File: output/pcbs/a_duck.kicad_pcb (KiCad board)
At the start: 2 copper layers, 135.1 x 107.9 mm, 38 parts

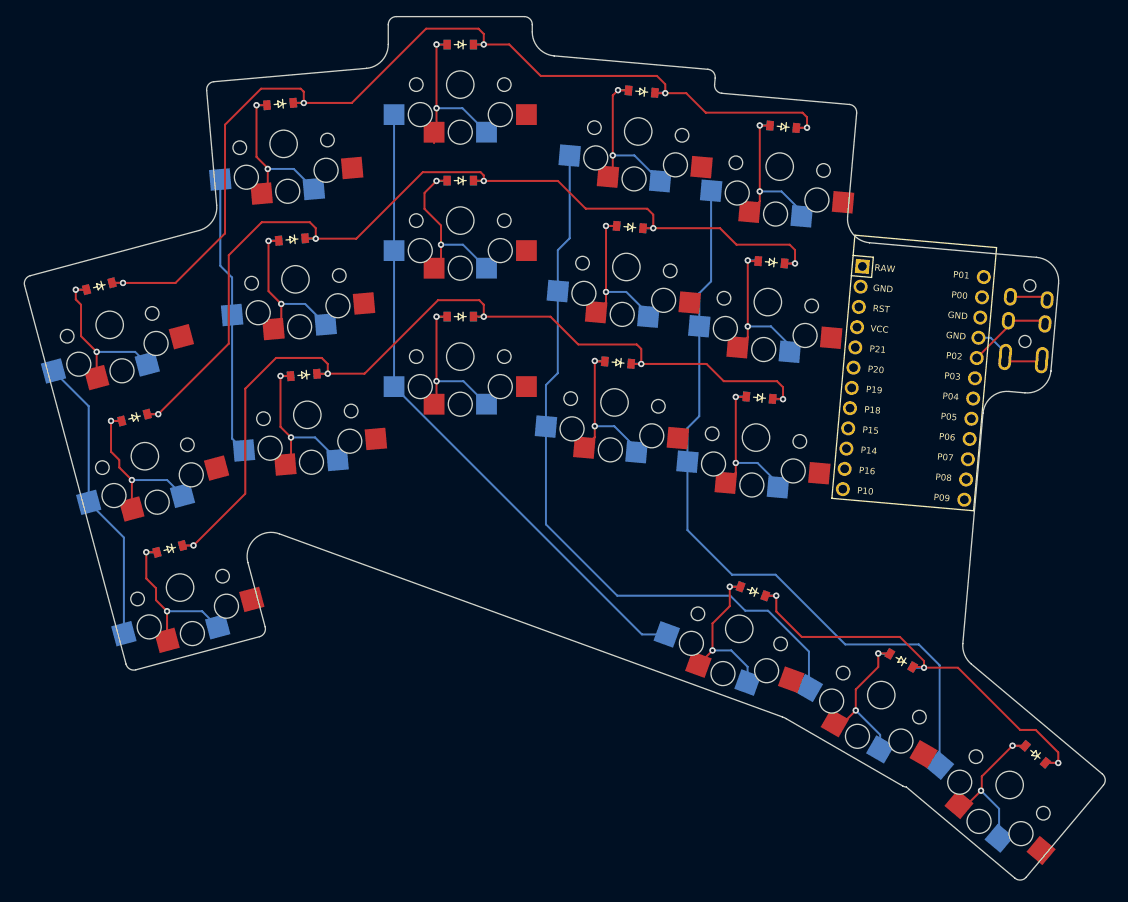
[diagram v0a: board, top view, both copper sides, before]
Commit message: Fix outlines / edge cuts of PCB
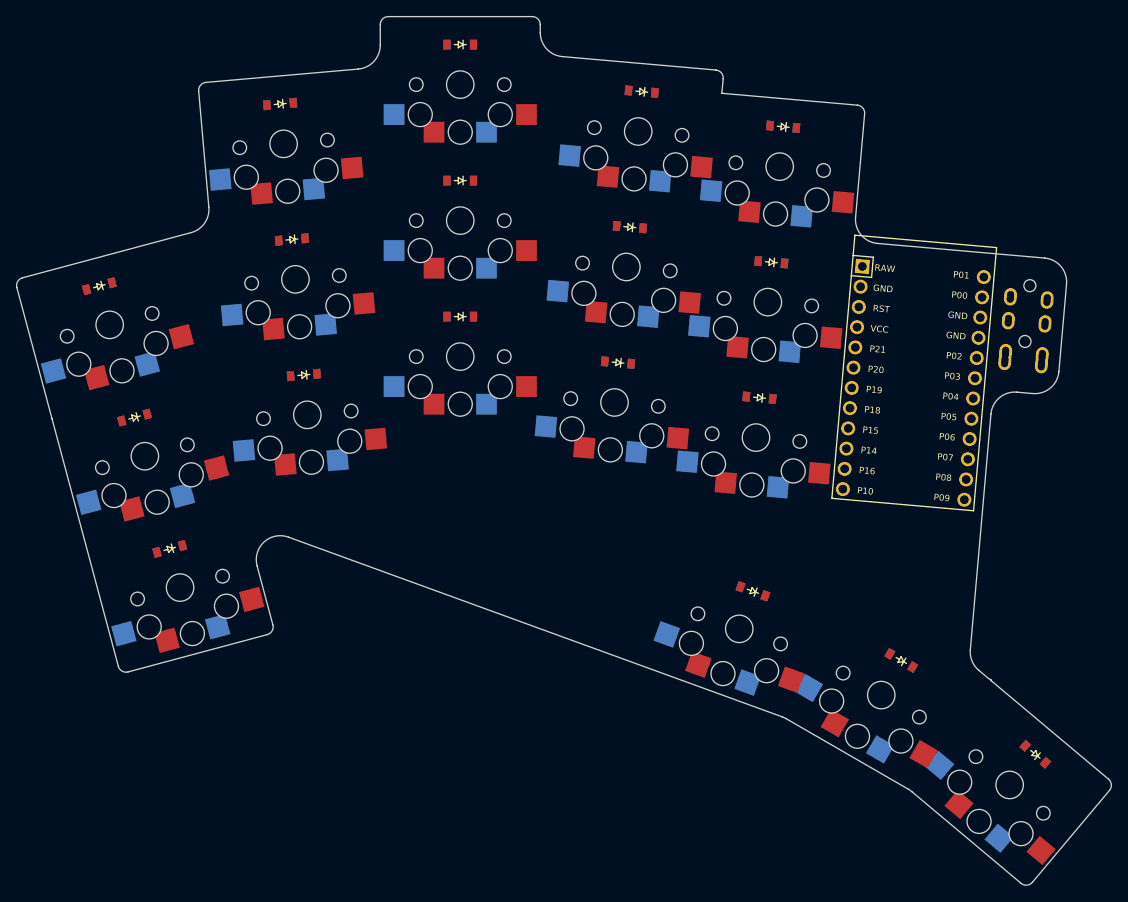
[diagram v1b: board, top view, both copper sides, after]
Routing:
- net P15: track 129.8 -> 0.00 mm, vias 5 -> 0
- net P14: track 121.9 -> 0.00 mm, vias 5 -> 0
- net P16: track 118.3 -> 0.00 mm, vias 5 -> 0
- net P5: track 94.7 -> 0.00 mm
- net P6: track 91.3 -> 0.00 mm
- net P7: track 81.3 -> 0.00 mm
- net P10: track 55.2 -> 0.00 mm, vias 3 -> 0
- net P9: track 38.2 -> 0.00 mm
- net P8: track 35.1 -> 0.00 mm
- net middle_top: track 24.3 -> 0.00 mm, vias 2 -> 0
- net middle_home: track 23.4 -> 0.00 mm, vias 2 -> 0
- net pinky_bottom: track 23.3 -> 0.00 mm, vias 2 -> 0
- net middle_bottom: track 22.9 -> 0.00 mm, vias 2 -> 0
- net pinky_home: track 21.9 -> 0.00 mm, vias 2 -> 0
- net pinky_top: track 21.7 -> 0.00 mm, vias 2 -> 0
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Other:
- board size 135.1 x 107.9 mm -> 136.8 x 108.6 mm

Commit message: Fix left side pins for easier routing
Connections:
- D1 pad 1: P16 -> P14
- D10 pad 1: P16 -> P14
- D11 pad 1: P14 -> P16
- D12 pad 1: P15 -> P10
- D13 pad 1: P16 -> P14
- D14 pad 1: P14 -> P16
- D15 pad 1: P15 -> P10
- D16 pad 1: P10 -> P15
- D17 pad 1: P10 -> P15
- D18 pad 1: P10 -> P15
- D2 pad 1: P14 -> P16
- D3 pad 1: P15 -> P10
- D4 pad 1: P16 -> P14
- D5 pad 1: P14 -> P16
- D6 pad 1: P15 -> P10
- D7 pad 1: P16 -> P14
- D8 pad 1: P14 -> P16
- D9 pad 1: P15 -> P10

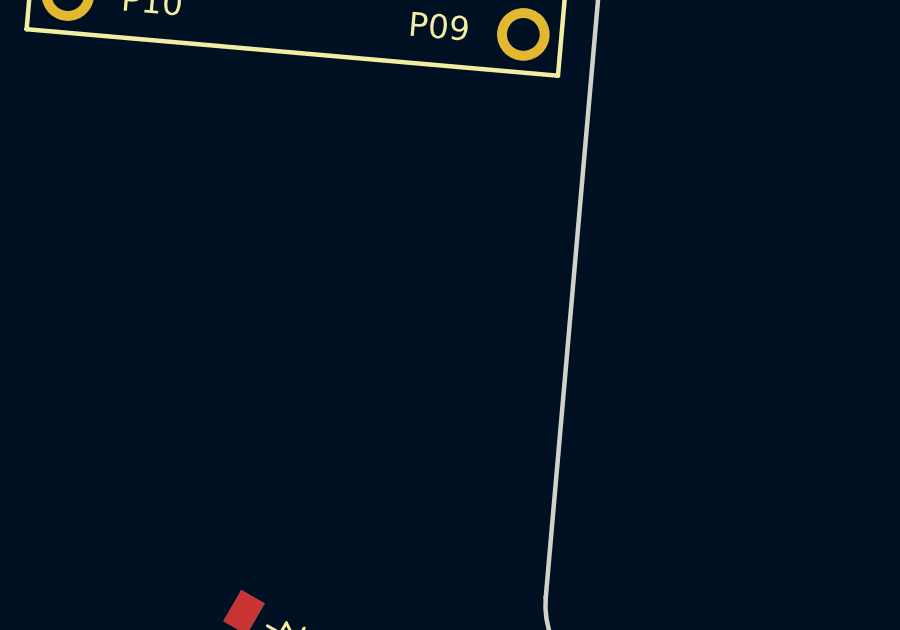
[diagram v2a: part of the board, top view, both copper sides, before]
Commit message: Added SMD reset button
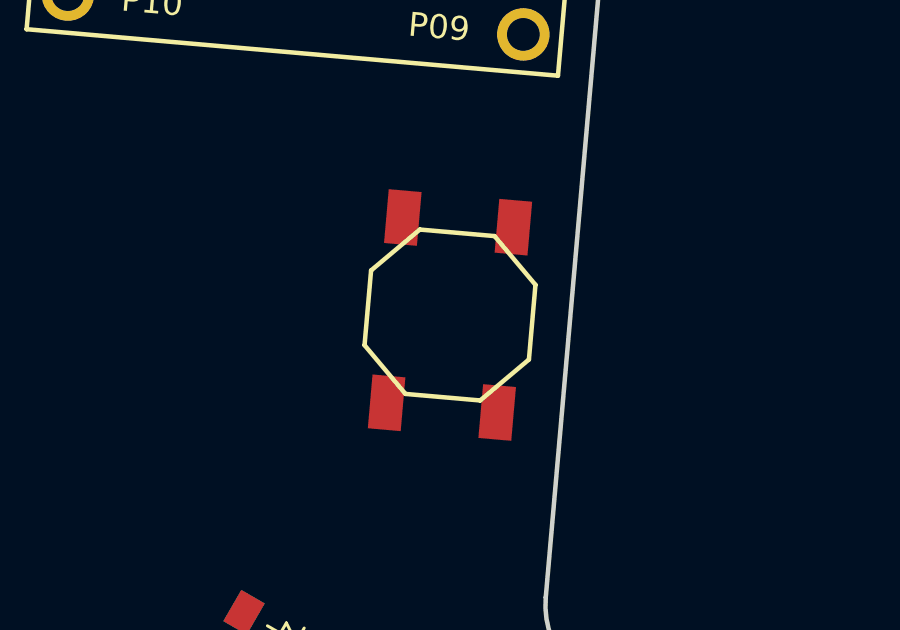
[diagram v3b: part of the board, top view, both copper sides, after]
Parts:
- added B1: , E73:SW_TACT_ALPS_SKQGABE010, F.Cu at (109.2, -1.05)
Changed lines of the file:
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@@
         (pad 24 thru_hole circle (at 13.97 -7.62 0) (size 1.7526 1.7526) (drill 1.0922) (layers *.Cu *.SilkS *.Mask) (net 2 "P9"))
       )
+    (module E73:SW_TACT_ALPS_SKQGABE010 (layer F.Cu)
+        (descr "Low-profile SMD Tactile Switch, https://www.e-switch.com/product-catalog/tact/product-lines/tl3342-series-low-profile-smt-tact-switch")
+        (tags "SPST Tactile Switch")
+        (at 109.1881054 -1.048862800000002 -95)
+        (fp_text reference "B1" (at 0 0) (layer F.SilkS) hide (effects (font (size 1.27 1.27) (thickness 0.15))))
+        (fp_text value "" (at 0 0) (layer F.SilkS) hide (effects (font (size 1.27 1.27) (thickness 0.15))))
+        (fp_line (start 2.75 1.25) (end 1.25 2.75) (layer F.SilkS) (width 0.15))
+        (fp_line (start 2.75 -1.25) (end 1.25 -2.75) (layer F.SilkS) (width 0.15))
+        (fp_line (start 2.75 -1.25) (end 2.75 1.25) (layer F.SilkS) (width 0.15))
+        (fp_line (start -1.25 2.75) (end 1.25 2.75) (layer F.SilkS) (width 0.15))
+        (fp_line (start -1.25 -2.75) (end 1.25 -2.75) (layer F.SilkS) (width 0.15))
+        (fp_line (start -2.75 1.25) (end -1.25 2.75) (layer F.SilkS) (width 0.15))
+        (fp_line (start -2.75 -1.25) (end -1.25 -2.75) (layer F.SilkS) (width 0.15))
+        (fp_line (start -2.75 -1.25) (end -2.75 1.25) (layer F.SilkS) (width 0.15))
+        (pad 1 smd rect (at -3.1 -1.85 -95) (size 1.8 1.1) (layers F.Cu F.Paste F.Mask) (net 29 "GND"))
+        (pad 1 smd rect (at 3.1 -1.85 -95) (size 1.8 1.1) (layers F.Cu F.Paste F.Mask) (net 29 "GND"))
+        (pad 2 smd rect (at -3.1 1.85 -95) (size 1.8 1.1) (layers F.Cu F.Paste F.Mask) (net 30 "RST"))
+        (pad 2 smd rect (at 3.1 1.85 -95) (size 1.8 1.1) (layers F.Cu F.Paste F.Mask) (net 30 "RST"))
+    )
       (module TRRS-PJ-320A-dual (layer F.Cu)
       (at 122.2564998 -38.552590200000004 -5)
